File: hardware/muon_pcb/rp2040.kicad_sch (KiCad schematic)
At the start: 38 parts, among them J4 Micro_SD_Card_Det1, J5 Conn_01x02_Pin, SW4 SW_Push_Shielded, SW5 SW_Push_Shielded, U12 RP2040, U3 W25Q128JVS, Y3 ABM8-272-T3

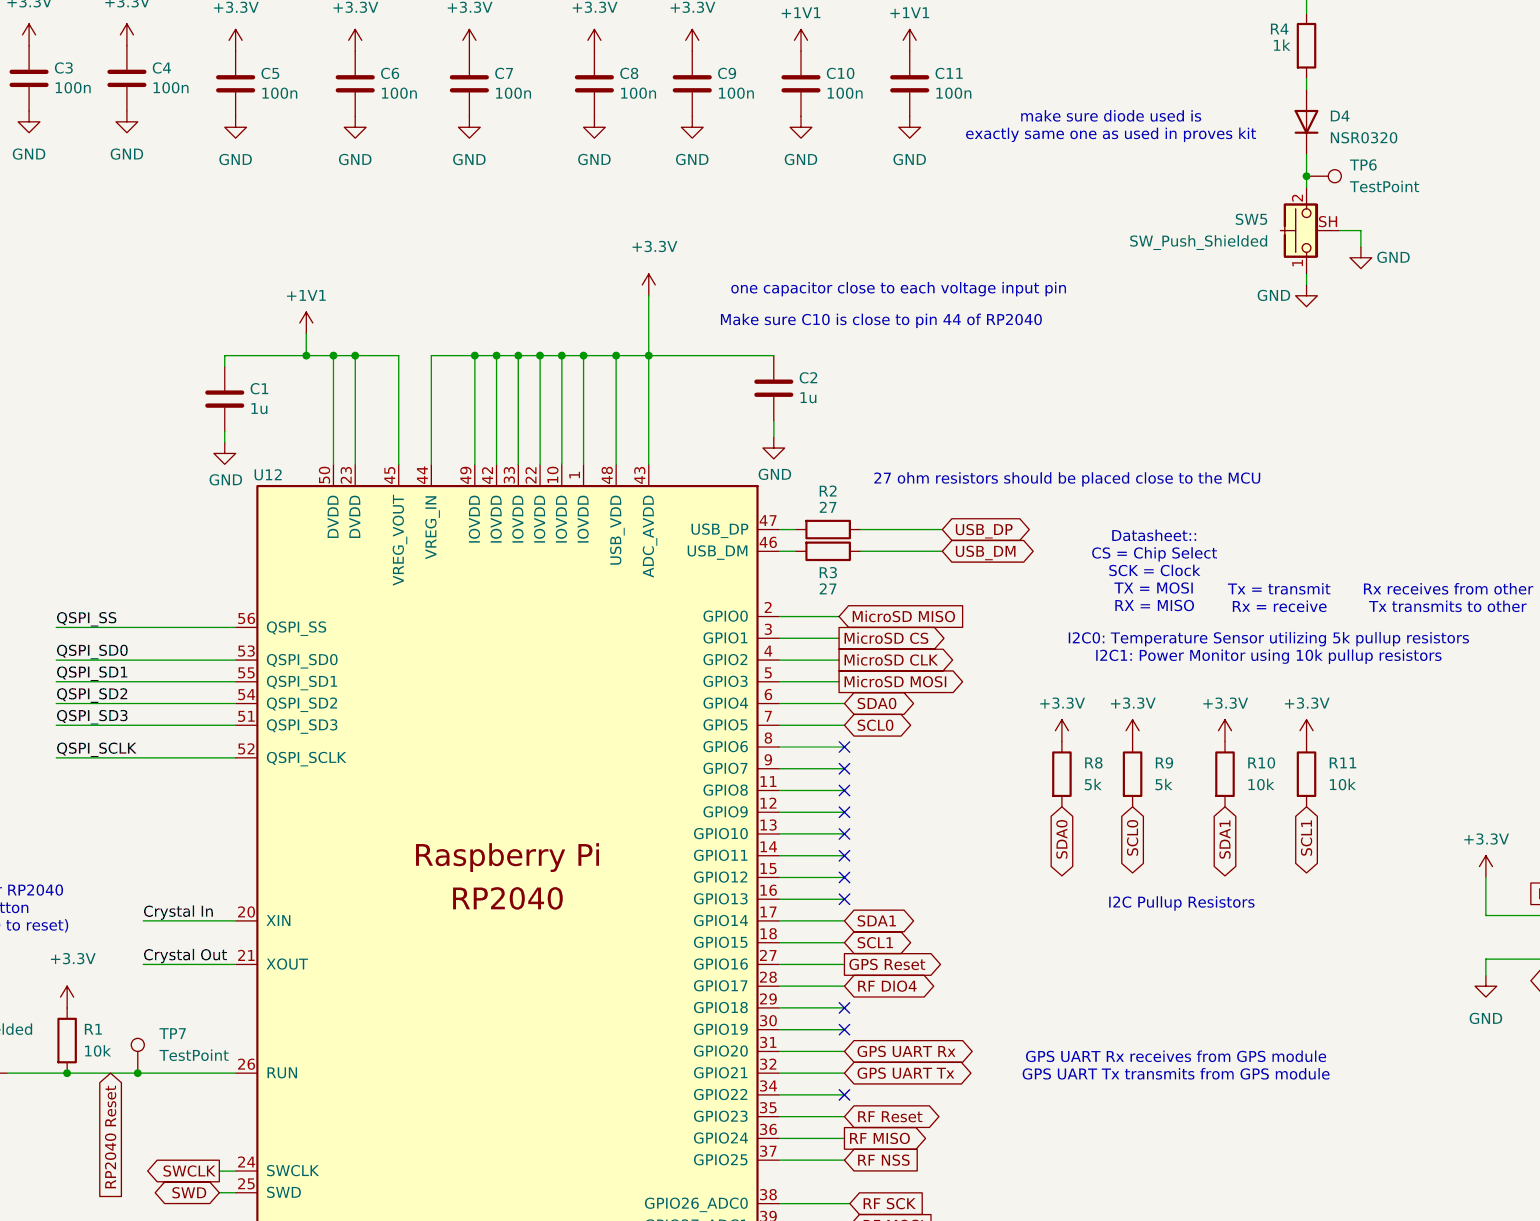
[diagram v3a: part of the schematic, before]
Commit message: finished assigning bouni tool jlcpcb parts & layout should match components and be good to go
final review
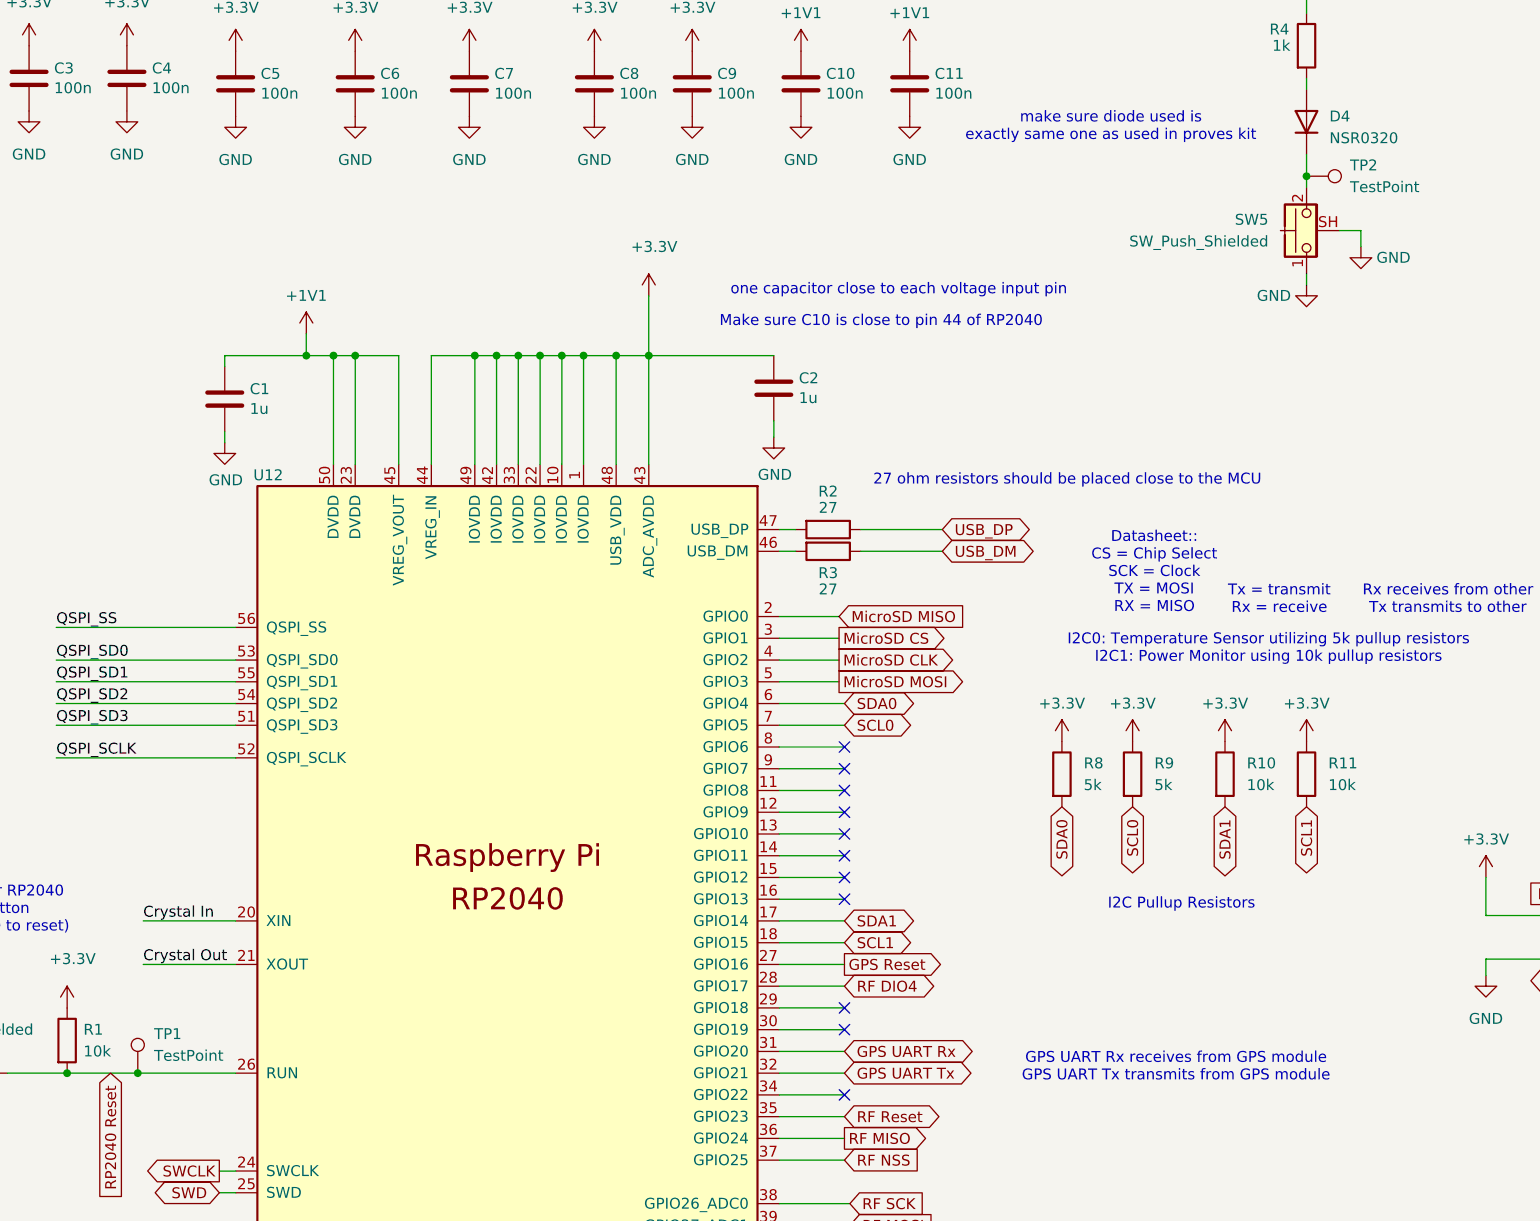
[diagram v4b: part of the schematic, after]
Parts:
- J5: footprint Connector_PinHeader_1.00mm:PinHeader_1x02_P1.00mm_Vertical -> 1my_footprints:HDR-TH_2P-P2.54-V-M
- TP1: renamed from TP7; footprint 1my_footprints:TestPoint_Loop_D1.80mm_Drill1.0mm_Beaded -> 1my_footprints:TH_BD3.2-D2.0
- TP2: renamed from TP6; footprint 1my_footprints:TestPoint_Loop_D1.80mm_Drill1.0mm_Beaded -> 1my_footprints:TH_BD3.2-D2.0
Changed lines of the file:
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@@
 			)
 		)
-		(property "Footprint" "Connector_PinHeader_1.00mm:PinHeader_1x02_P1.00mm_Vertical"
+		(property "Footprint" "1my_footprints:HDR-TH_2P-P2.54-V-M"
 			(at 30.48 180.975 0)
 			(effects
@@
 		(dnp no)
 		(fields_autoplaced yes)
-		(property "Reference" "TP6"
+		(property "Reference" "TP2"
 			(at 184.15 43.1799 90)
 			(effects
@@
 			)
 		)
-		(property "Footprint" "1my_footprints:TestPoint_Loop_D1.80mm_Drill1.0mm_Beaded"
+		(property "Footprint" "1my_footprints:TH_BD3.2-D2.0"
 			(at 179.07 49.53 0)
 			(effects
@@
 			(project ""
 				(path "/e4ef350a-b140-44e0-8bc3-973fc24bf90a/06e07132-39d3-4769-b65c-2c1064b388d8"
-					(reference "TP6")
+					(reference "TP2")
 					(unit 1)
 				)
@@
 		(dnp no)
 		(fields_autoplaced yes)
-		(property "Reference" "TP7"
-			(at 45.085 144.6529 0)
+		(property "Reference" "TP1"
+			(at 44.45 144.6529 0)
 			(effects
 				(font
@@
 		)
 		(property "Value" "TestPoint"
-			(at 45.085 147.1929 0)
+			(at 44.45 147.1929 0)
 			(effects
 				(font
@@
 			)
 		)
-		(property "Footprint" "1my_footprints:TestPoint_Loop_D1.80mm_Drill1.0mm_Beaded"
+		(property "Footprint" "1my_footprints:TH_BD3.2-D2.0"
 			(at 47.625 149.225 0)
 			(effects
@@
 			(project "og_pcb"
 				(path "/e4ef350a-b140-44e0-8bc3-973fc24bf90a/06e07132-39d3-4769-b65c-2c1064b388d8"
-					(reference "TP7")
+					(reference "TP1")
 					(unit 1)
 				)

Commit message: final one maybe
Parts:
- H1, H2: symbol Mechanical:MountingHole -> Mechanical:MountingHole_Pad
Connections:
- net GND: now also H1.1, H2.1
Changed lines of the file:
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@@
 	)
 	(junction
+		(at 159.385 177.165)
+		(diameter 0)
+		(color 0 0 0 0)
+	)
+	(junction
 		(at 89.535 65.405)
 		(diameter 0)
@@
 	(wire
 		(pts
+			(xy 154.305 174.625) (xy 154.305 177.165)
+		)
+		(stroke
+			(width 0)
+			(type default)
+		)
+	)
+	(wire
+		(pts
 			(xy 33.02 97.155) (xy 53.975 97.155)
 		)
@@
 	(wire
 		(pts
+			(xy 164.465 177.165) (xy 159.385 177.165)
+		)
+		(stroke
+			(width 0)
+			(type default)
+		)
+	)
+	(wire
+		(pts
 			(xy 92.075 78.105) (xy 92.075 65.405)
 		)
@@
 	(wire
 		(pts
+			(xy 125.73 172.085) (xy 117.475 172.085)
+		)
+		(stroke
+			(width 0)
+			(type default)
+		)
+	)
+	(wire
+		(pts
 			(xy 117.475 139.065) (xy 125.095 139.065)
 		)
@@
 	(wire
 		(pts
+			(xy 164.465 174.625) (xy 164.465 177.165)
+		)
+		(stroke
+			(width 0)
+			(type default)
+		)
+	)
+	(wire
+		(pts
 			(xy 117.475 156.845) (xy 125.095 156.845)
 		)
@@
 	(wire
 		(pts
+			(xy 154.305 177.165) (xy 159.385 177.165)
+		)
+		(stroke
+			(width 0)
+			(type default)
+		)
+	)
+	(wire
+		(pts
 			(xy 223.52 62.865) (xy 234.95 62.865)
 		)
@@
 	(global_label "Cosmic Analog"
 		(shape input)
-		(at 117.475 172.085 0)
+		(at 125.73 172.085 0)
 		(fields_autoplaced yes)
 		(effects
@@
 		)
 		(property "Intersheetrefs" "${INTERSHEET_REFS}"
-			(at 134.6114 172.085 0)
+			(at 142.8664 172.085 0)
 			(effects
 				(font
@@
 	)
 	(symbol
-		(lib_id "Mechanical:MountingHole")
-		(at 156.21 180.34 0)
+		(lib_id "Mechanical:MountingHole_Pad")
+		(at 154.305 172.085 0)
 		(unit 1)
 		(exclude_from_sim yes)
@@
 		(fields_autoplaced yes)
 		(property "Reference" "H2"
-			(at 158.75 179.0699 0)
+			(at 156.845 169.5449 0)
 			(effects
 				(font
@@
 		)
 		(property "Value" "MountingHole"
-			(at 158.75 181.6099 0)
+			(at 156.845 172.0849 0)
 			(effects
 				(font
@@
 		)
 		(property "Footprint" ""
-			(at 156.21 180.34 0)
+			(at 154.305 172.085 0)
 			(effects
 				(font
@@
 		)
 		(property "Datasheet" "~"
-			(at 156.21 180.34 0)
+			(at 154.305 172.085 0)
 			(effects
 				(font
@@
 			)
 		)
-		(property "Description" "Mounting Hole without connection"
-			(at 156.21 180.34 0)
+		(property "Description" "Mounting Hole with connection"
+			(at 154.305 172.085 0)
 			(effects
 				(font
@@
 			)
 		)
+		(pin "1"
+		)
 		(instances
 			(project "og_pcb"
@@
 	)
 	(symbol
-		(lib_id "Mechanical:MountingHole")
-		(at 156.21 173.355 0)
+		(lib_id "Mechanical:MountingHole_Pad")
+		(at 164.465 172.085 0)
 		(unit 1)
 		(exclude_from_sim yes)
@@
 		(fields_autoplaced yes)
 		(property "Reference" "H1"
-			(at 158.75 172.0849 0)
+			(at 167.005 169.5449 0)
 			(effects
 				(font
@@
 		)
 		(property "Value" "MountingHole"
-			(at 158.75 174.6249 0)
+			(at 167.005 172.0849 0)
 			(effects
 				(font
@@
 		)
 		(property "Footprint" ""
-			(at 156.21 173.355 0)
+			(at 164.465 172.085 0)
 			(effects
 				(font
@@
 		)
 		(property "Datasheet" "~"
-			(at 156.21 173.355 0)
+			(at 164.465 172.085 0)
 			(effects
 				(font
@@
 			)
 		)
-		(property "Description" "Mounting Hole without connection"
-			(at 156.21 173.355 0)
+		(property "Description" "Mounting Hole with connection"
+			(at 164.465 172.085 0)
 			(effects
 				(font
@@
 			)
 		)
+		(pin "1"
+		)
 		(instances
 			(project ""
@@
 					(unit 1)
 				)
+			)
+		)
+	)
+	(symbol
+		(lib_id "power:GND")
+		(at 159.385 177.165 0)
+		(unit 1)
+		(exclude_from_sim no)
+		(in_bom yes)
+		(on_board yes)
+		(dnp no)
+		(fields_autoplaced yes)
+		(property "Reference" "#PWR03"
+			(at 159.385 183.515 0)
+			(effects
+				(font
+					(size 1.27 1.27)
+				)
+				(hide yes)
+			)
+		)
+		(property "Value" "GND"
+			(at 159.385 181.61 0)
+			(effects
+				(font
+					(size 1.27 1.27)
+				)
+			)
+		)
+		(property "Footprint" ""
+			(at 159.385 177.165 0)
+			(effects
+				(font
+					(size 1.27 1.27)
+				)
+				(hide yes)
+			)
+		)
+		(property "Datasheet" ""
+			(at 159.385 177.165 0)
+			(effects
+				(font
+					(size 1.27 1.27)
+				)
+				(hide yes)
+			)
+		)
+		(property "Description" "Power symbol creates a global label with name \"GND\" , ground"
+			(at 159.385 177.165 0)
+			(effects
+				(font
+					(size 1.27 1.27)
+				)
+				(hide yes)
+			)
+		)
+		(pin "1"
+		)
+		(instances
+			(project ""
+				(path "/e4ef350a-b140-44e0-8bc3-973fc24bf90a/06e07132-39d3-4769-b65c-2c1064b388d8"
+					(reference "#PWR03")
+					(unit 1)
+				)

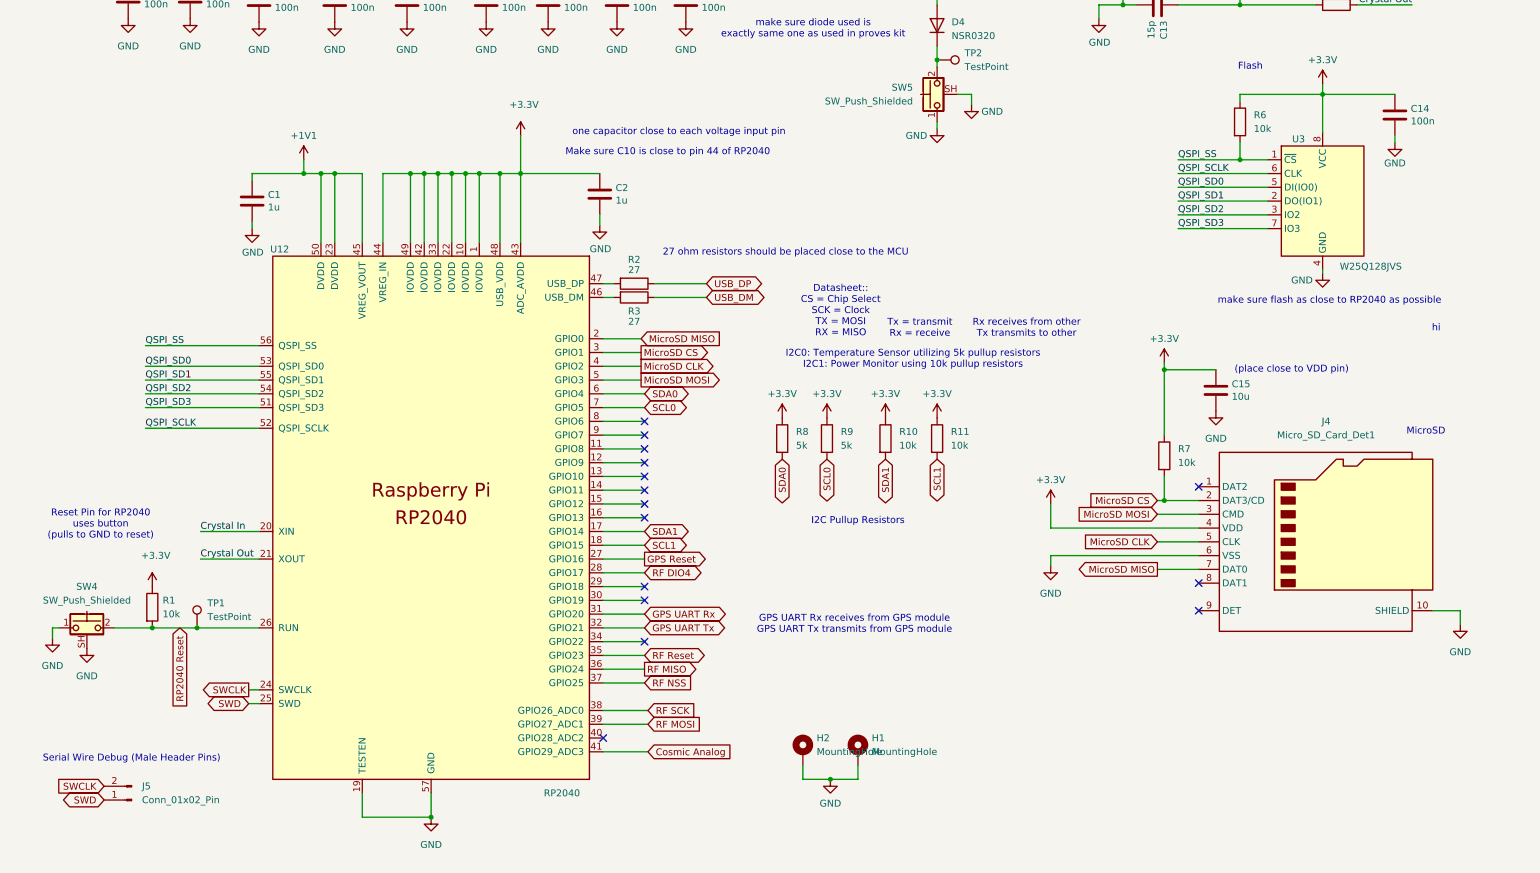
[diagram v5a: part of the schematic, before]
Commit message: uploaded pcb with gps 1pps implemented and cygnet logo
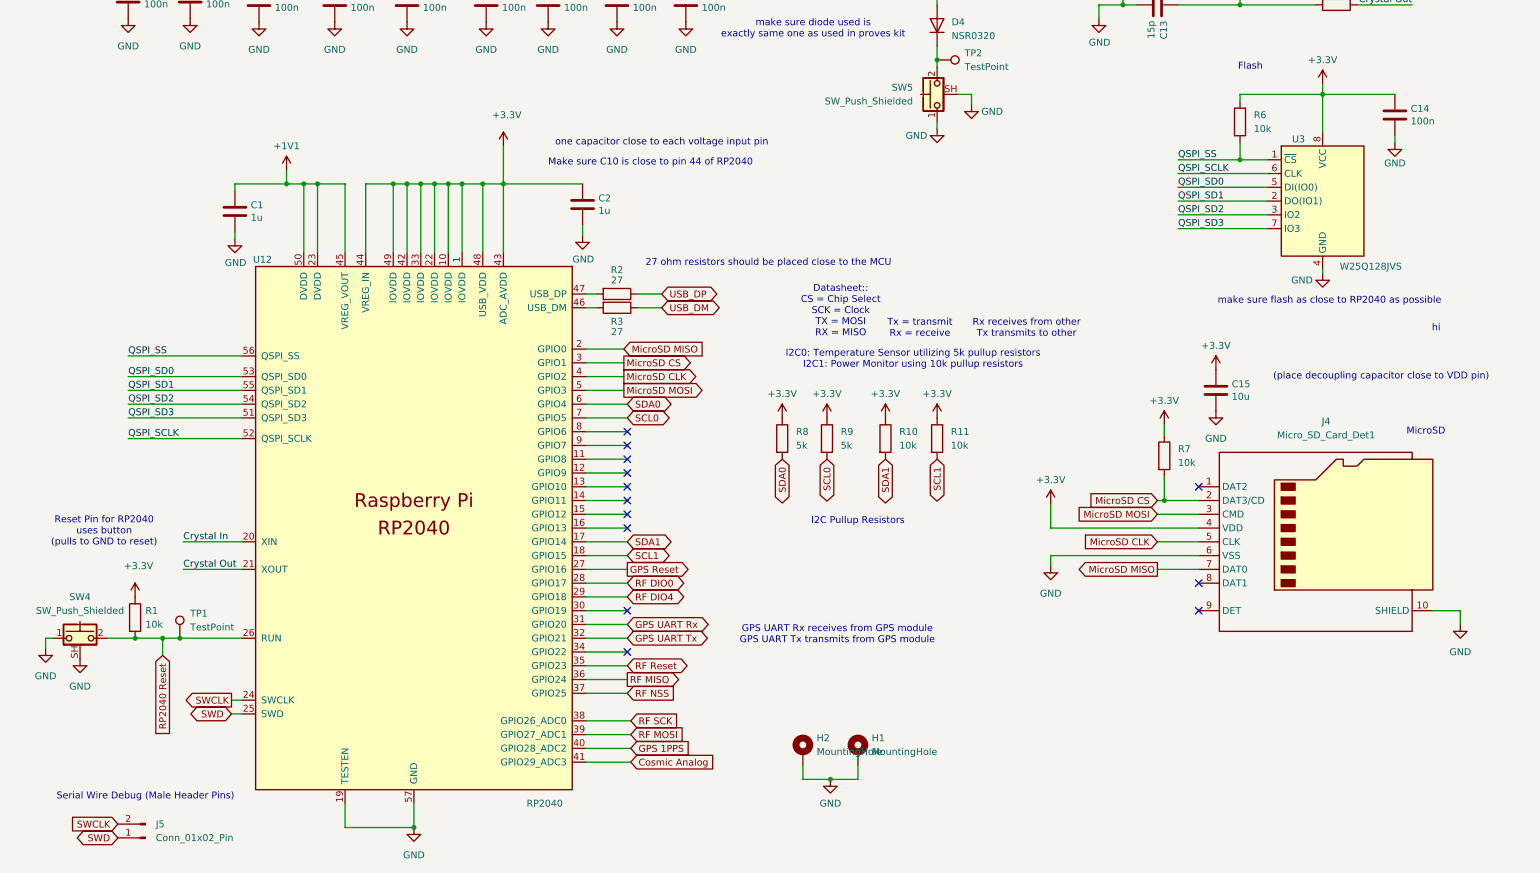
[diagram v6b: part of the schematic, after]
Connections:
- net RF DIO4: now also U12.29 (GPIO18); no longer U12.28 (GPIO17)
- net GPS 1PPS: now reaches U12.40 (GPIO28_ADC2)
- new net RF DIO0: U12.28 (GPIO17)
- no-connect marks 15 -> 13
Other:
- note added: "(place decoupling capacitor close to VDD pin)"
- note removed: "(place close to VDD pin)"
- moved on the sheet: C1, C2, J5, R1, R2, R3, SW4, TP1, U12

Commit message: uploaded cleaner schematic
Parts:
- removed H1, H2: MountingHole, symbol Mechanical:MountingHole_Pad
- added H1, H2: MountingHole, symbol Mechanical:MountingHole
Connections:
- net RF MOSI: now also U12.35 (GPIO23); no longer U12.39 (GPIO27_ADC1)
- net RF Reset: now also U12.39 (GPIO27_ADC1); no longer U12.35 (GPIO23)
- net GPS UART Rx renamed MCU UART Tx
- net GPS UART Tx renamed MCU UART Rx
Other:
- note added: "Decoupling Capacitors (1.1V)"
- note added: "Decoupling Capacitors (3.3V)"
- note added: "Flash Memory"
- note added: "RP2040 Microcontroller"
- note removed: "Decoupling Capacitors"
- note removed: "Flash"
- note removed: "GPS UART Rx receives from GPS module GPS UART Tx transmits from GPS module"
- moved on the sheet: C1, C10, C11, C12, C13, C14, C15, C2, C3, C4, C5, C6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
